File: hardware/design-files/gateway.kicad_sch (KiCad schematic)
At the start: 0 parts

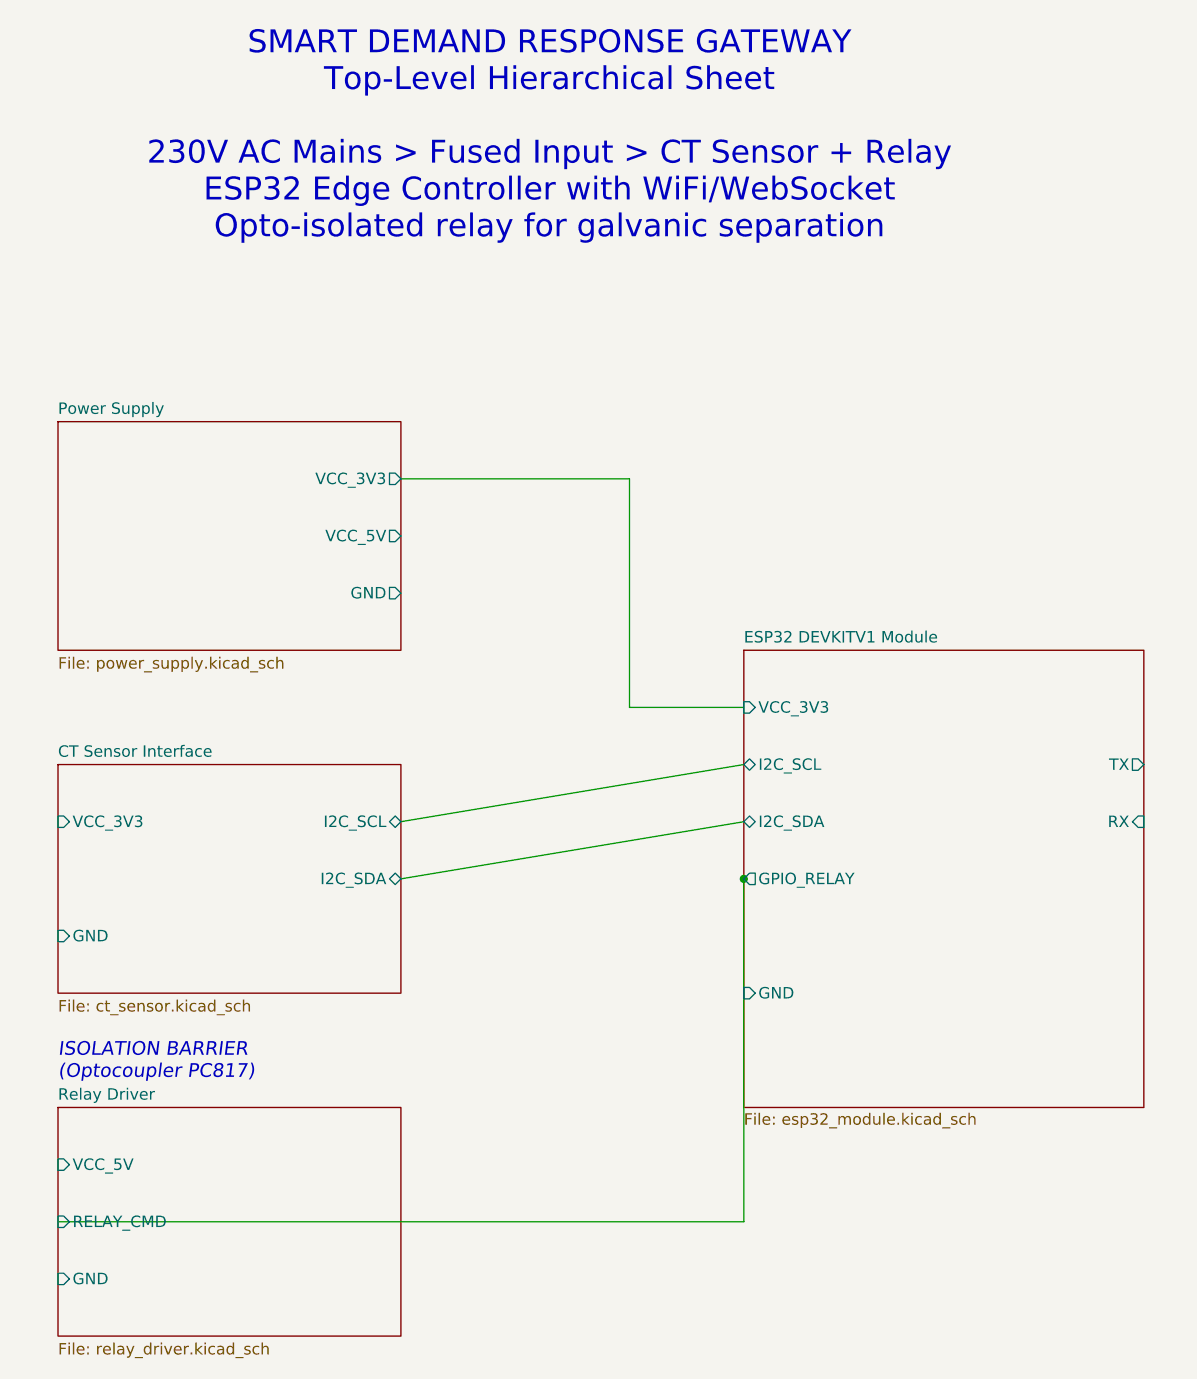
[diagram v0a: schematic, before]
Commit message: feat(hardware): update KiCad schematics with component symbols and layout refinements
- Add ADS1115 16-bit I2C ADC symbol to CT sensor schematic
- Add AudioJack2 connector symbol for analog signal input
- Update ESP32 module schematic with refined pin configurations
- Update power supply schematic with improved component placement
- Update relay driver schematic with optimized routing
- Refine PCB layout in gateway.kicad_pcb with better trace routing
- Update project settings in gateway.kicad_pro for design rule compliance
- Add project rules configuration in gateway.kicad_prl for manufacturing constraints
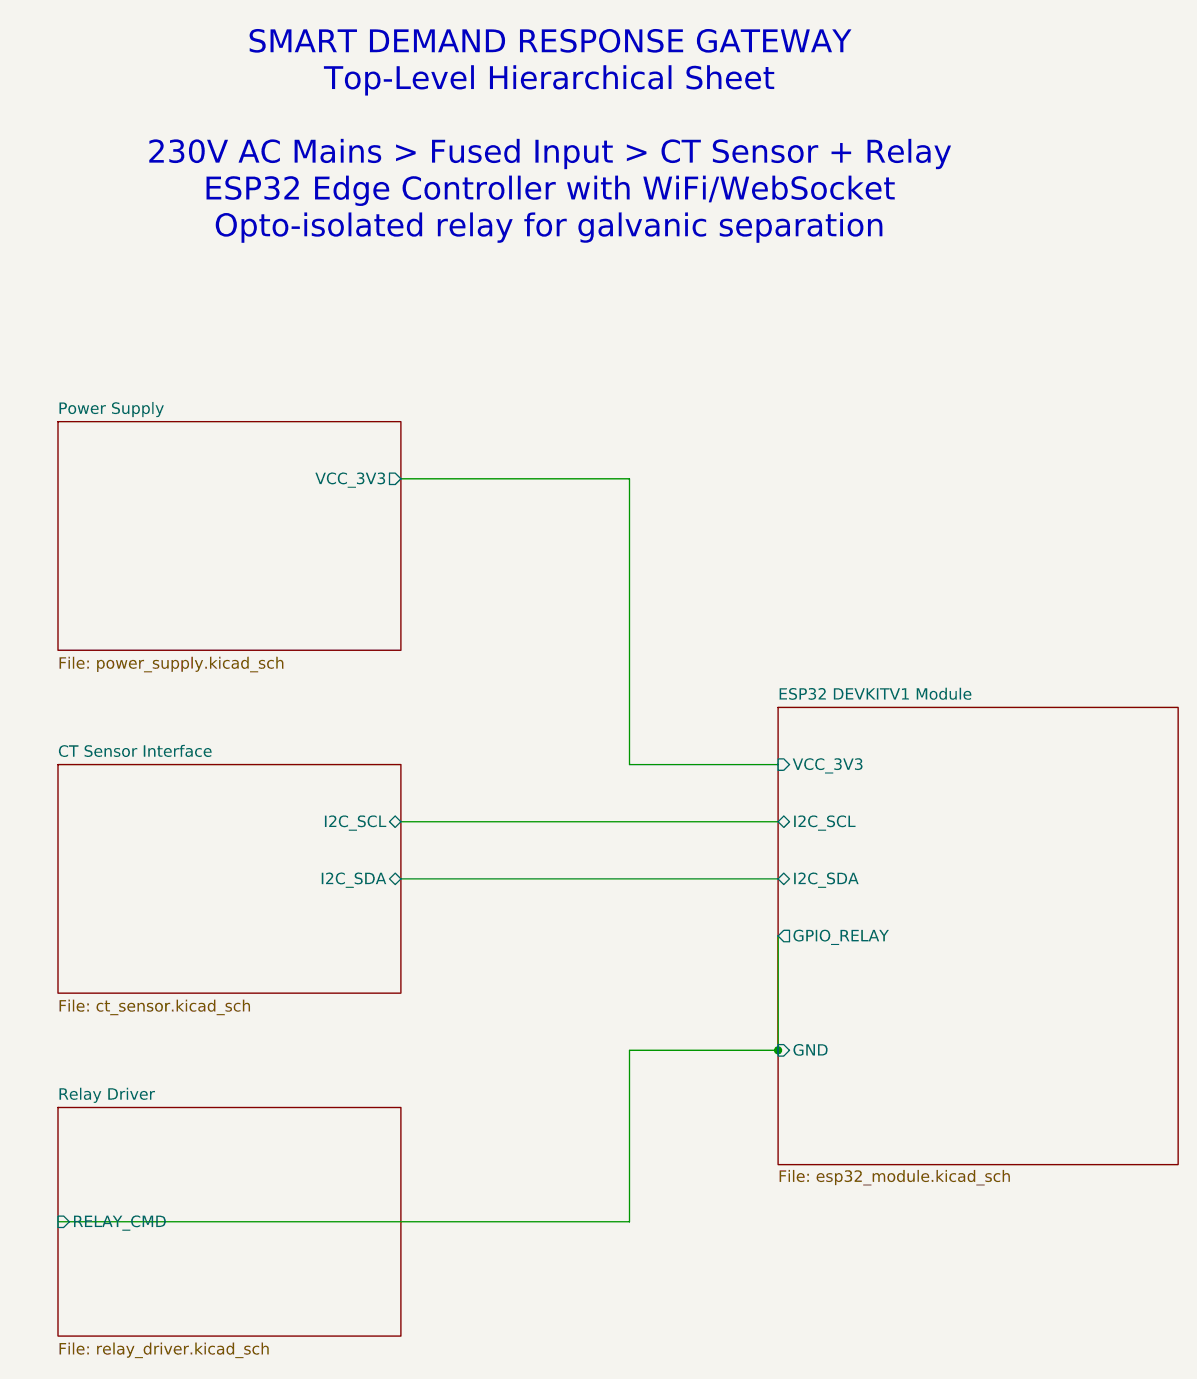
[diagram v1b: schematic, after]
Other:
- sheet CT Sensor Interface ports: added none; removed GND, VCC_3V3
- sheet ESP32 DEVKITV1 Module ports: added none; removed RX, TX
- sheet Power Supply ports: added none; removed GND, VCC_5V
- sheet Relay Driver ports: added none; removed GND, VCC_5V
- note removed: "ISOLATION BARRIER (Optocoupler PC817)"
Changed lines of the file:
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@@
-		)
-	)
-	(text "ISOLATION BARRIER\n(Optocoupler PC817)"
-		(exclude_from_sim no)
-		(at 46.99 140.97 0)
-		(effects
-			(font
-				(size 1.524 1.524)
-				(italic yes)
-			)
-			(justify left)
 		)
 	)
 	(junction
-		(at 123.19 120.65)
+		(at 127 139.7)
 		(diameter 0)
 		(color 0 0 0 0)
@@
 	(wire
 		(pts
-			(xy 110.49 76.2) (xy 110.49 101.6)
-		)
-		(stroke
-			(width 0)
-			(type default)
-		)
-	)
-	(wire
-		(pts
-			(xy 85.09 114.3) (xy 123.19 107.95)
+			(xy 110.49 76.2) (xy 110.49 107.95)
+		)
+		(stroke
+			(width 0)
+			(type default)
+		)
+	)
+	(wire
+		(pts
+			(xy 110.49 139.7) (xy 127 139.7)
+		)
+		(stroke
+			(width 0)
+			(type default)
+		)
+	)
+	(wire
+		(pts
+			(xy 110.49 139.7) (xy 110.49 158.75)
+		)
+		(stroke
+			(width 0)
+			(type default)
+		)
+	)
+	(wire
+		(pts
+			(xy 85.09 114.3) (xy 127 114.3)
 		)
 		(stroke
@@
 	(wire
 		(pts
-			(xy 85.09 120.65) (xy 123.19 114.3)
-		)
-		(stroke
-			(width 0)
-			(type default)
-		)
-	)
-	(wire
-		(pts
-			(xy 123.19 120.65) (xy 123.19 158.75)
-		)
-		(stroke
-			(width 0)
-			(type default)
-		)
-	)
-	(wire
-		(pts
-			(xy 123.19 158.75) (xy 46.99 158.75)
-		)
-		(stroke
-			(width 0)
-			(type default)
-		)
-	)
-	(wire
-		(pts
-			(xy 110.49 101.6) (xy 123.19 101.6)
+			(xy 85.09 120.65) (xy 127 120.65)
+		)
+		(stroke
+			(width 0)
+			(type default)
+		)
+	)
+	(wire
+		(pts
+			(xy 127 127) (xy 127 139.7)
+		)
+		(stroke
+			(width 0)
+			(type default)
+		)
+	)
+	(wire
+		(pts
+			(xy 110.49 158.75) (xy 46.99 158.75)
+		)
+		(stroke
+			(width 0)
+			(type default)
+		)
+	)
+	(wire
+		(pts
+			(xy 110.49 107.95) (xy 127 107.95)
 		)
 		(stroke
@@
 			)
 		)
-		(pin "VCC_5V" output
-			(at 85.09 82.55 0)
-			(effects
-				(font
-					(size 1.27 1.27)
-				)
-				(justify left)
-			)
-		)
-		(pin "GND" output
-			(at 85.09 88.9 0)
-			(effects
-				(font
-					(size 1.27 1.27)
-				)
-				(justify left)
-			)
-		)
 		(instances
 			(project "gateway"
@@
 			)
 		)
-		(pin "VCC_3V3" input
-			(at 46.99 114.3 180)
-			(effects
-				(font
-					(size 1.27 1.27)
-				)
-				(justify right)
-			)
-		)
-		(pin "GND" input
-			(at 46.99 127 180)
-			(effects
-				(font
-					(size 1.27 1.27)
-				)
-				(justify right)
-			)
-		)
 		(instances
 			(project "gateway"
@@
 			)
 		)
-		(pin "VCC_5V" input
-			(at 46.99 152.4 180)
-			(effects
-				(font
-					(size 1.27 1.27)
-				)
-				(justify right)
-			)
-		)
-		(pin "GND" input
-			(at 46.99 165.1 180)
-			(effects
-				(font
-					(size 1.27 1.27)
-				)
-				(justify right)
-			)
-		)
 		(instances
 			(project "gateway"
@@
 	)
 	(sheet
-		(at 123.19 95.25)
+		(at 127 101.6)
 		(size 44.45 50.8)
 		(exclude_from_sim no)
@@
 		)
 		(property "Sheetname" "ESP32 DEVKITV1 Module"
-			(at 123.19 94.5384 0)
+			(at 127 100.8884 0)
 			(show_name no)
 			(do_not_autoplace no)
@@
 		)
 		(property "Sheetfile" "esp32_module.kicad_sch"
-			(at 123.19 146.6346 0)
+			(at 127 152.9846 0)
 			(show_name no)
 			(do_not_autoplace no)
@@
 		)
 		(pin "I2C_SCL" bidirectional
-			(at 123.19 107.95 180)
+			(at 127 114.3 180)
 			(effects
 				(font
@@
 		)
 		(pin "I2C_SDA" bidirectional
-			(at 123.19 114.3 180)
+			(at 127 120.65 180)
 			(effects
 				(font
@@
 		)
 		(pin "GPIO_RELAY" output
-			(at 123.19 120.65 180)
+			(at 127 127 180)
 			(effects
 				(font
@@
 		)
 		(pin "VCC_3V3" input
-			(at 123.19 101.6 180)
+			(at 127 107.95 180)
 			(effects
 				(font
@@
 		)
 		(pin "GND" input
-			(at 123.19 133.35 180)
-			(effects
-				(font
-					(size 1.27 1.27)
-				)
-				(justify right)
-			)
-		)
-		(pin "TX" output
-			(at 167.64 107.95 0)
-			(effects
-				(font
-					(size 1.27 1.27)
-				)
-				(justify left)
-			)
-		)
-		(pin "RX" input
-			(at 167.64 114.3 0)
-			(effects
-				(font
+			(at 127 139.7 180)
+			(effects
+				(font

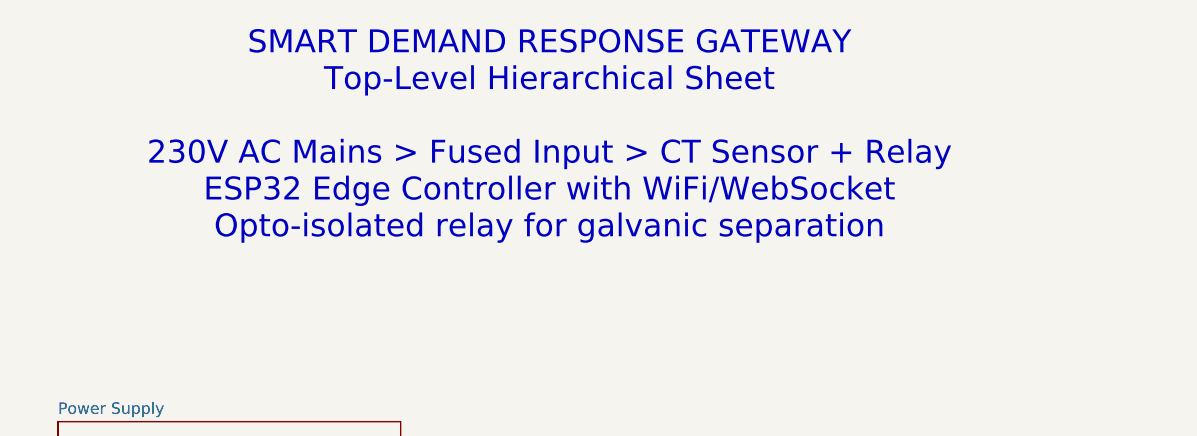
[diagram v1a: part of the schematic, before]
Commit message: feat(hardware): update PCB layout and component footprints
- Reposition ADS1115 ADC module on PCB (moved from 84.35,28 to 60.5,49.35 with 180° rotation)
- Update CT sensor connector footprint from PinHeader to 3.5mm audio jack (Switronic ST-005-G)
- Correct ESP32 module connector footprint from 1x02 to 1x06 pin header
- Regenerate component UUIDs and silk screen coordinates to reflect new placements
- Optimize PCB layout for improved signal routing and component accessibility
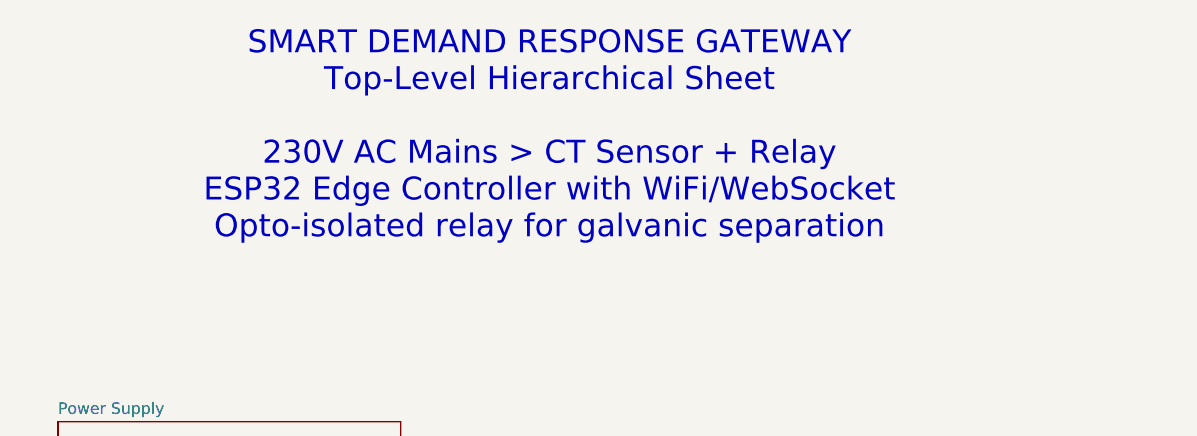
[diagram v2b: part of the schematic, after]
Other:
- note added: "SMART DEMAND RESPONSE GATEWAY Top-Level Hierarchical Sheet 230V AC Mains > CT Sensor + Relay ESP32 Edge Controller with WiFi/WebSocket Opto-isolated relay for galvanic separation"
- note removed: "SMART DEMAND RESPONSE GATEWAY Top-Level Hierarchical Sheet 230V AC Mains > Fused Input > CT Sensor + Relay ESP32 Edge Controller with WiFi/WebSocket Opto-isolated relay for galvanic separation"
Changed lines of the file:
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@@
 		(comment 4 "Open Source Hardware - MIT License")
 	)
-	(text "SMART DEMAND RESPONSE GATEWAY\nTop-Level Hierarchical Sheet\n\n230V AC Mains > Fused Input > CT Sensor + Relay\nESP32 Edge Controller with WiFi/WebSocket\nOpto-isolated relay for galvanic separation"
+	(text "SMART DEMAND RESPONSE GATEWAY\nTop-Level Hierarchical Sheet\n\n230V AC Mains > CT Sensor + Relay\nESP32 Edge Controller with WiFi/WebSocket\nOpto-isolated relay for galvanic separation"
 		(exclude_from_sim no)
 		(at 101.6 38.1 0)
